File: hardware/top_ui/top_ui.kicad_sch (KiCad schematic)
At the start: 20 parts, among them J2 J_STK_A, J3 J_STK_B, J5 ST7789 240x280, J6 Stern Klinke, Q1 BC847, Q2 P-FET 20V 1A, SW1 BTN1, SW2 BTN2, SW3 BTN3, SW4 BTN4, U2 SHT40-AD1B, U3 VL53L1X

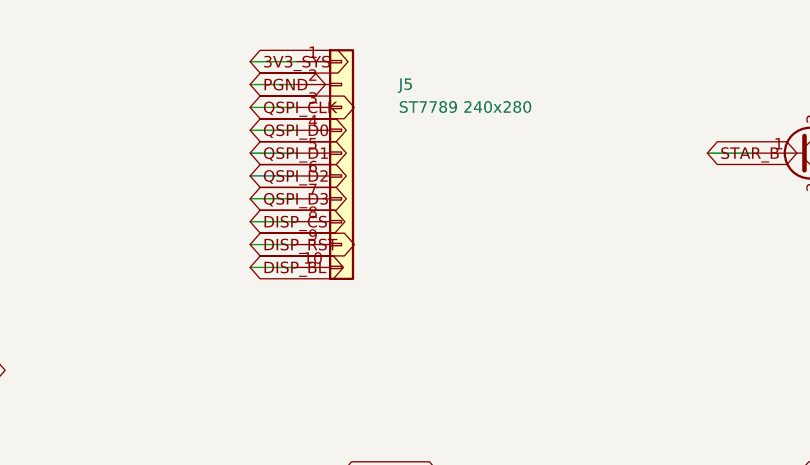
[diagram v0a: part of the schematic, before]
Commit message: Display gewaehlt: ER-TFT1.69-3, 12-polige FPC steckbar
  aktive Flaeche   27,97 x 32,63 mm
  sichtbar         28,97 x 33,63 mm
  Aussenmass       30,07 x 37,43 x 1,6 mm (FPC gefaltet)
  Treiber          ST7789V, 4-Draht-SPI

Quer eingebaut misst die aktive Flaeche 32,63 x 27,97 gegen ein Fenster von
32,70 x 27,00 - in der Breite bleiben 0,07 mm Luft, in der Hoehe verdeckt die
Zentralscheibe oben und unten je 0,49 mm. Rund acht Pixel je Seite, bewusst in
Kauf genommen. Die Firmware darf in diesen Zeilen nichts Wichtiges zeichnen.

Auf dem Top-Board passt es: 1,6 mm Dicke gegen 2,0 mm Budget, und in y reicht
das Panel nur bis +/-15,04 und bleibt damit frei von den Ecktastern bei
18,27..21,73. In x reicht es bis +/-18,71 und liegt NEBEN den Tastern, mit rund
1,5 mm diagonalem Abstand - das ist am realen Teil anzusehen.

J5 steht damit nicht mehr auf einem erfundenen 1,27-mm-Stiftleisten-Footprint
mit zehn Polen, sondern auf zwoelf Polen mit FPC-Buchse.

ZWEI ZAHLEN FEHLEN WEITERHIN, beide nur aus dem Datenblatt zu holen:

  Das RASTER der Fahne. Die Loetvariante ist mit 0,7 mm angegeben, und KiCad
  bringt fuer 0,7 mm kein einziges FPC-Footprint mit - nur 0,5 und 1,0. Ist es
  wirklich 0,7, muss eines in die Projektbibliothek gezeichnet werden. Bis
  dahin steht ein 0,5-mm-Footprint mit der richtigen Polzahl.

  Die PINBELEGUNG. Zwoelf Pole sind gesichert, welches Signal auf welchem
  liegt nicht. Die Zuordnung im Schaltplan ist die des alten Platzhalters und
  mit hoher Wahrscheinlichkeit falsch.

Beides steht so im Schaltplan-Generator, damit es niemand uebersieht: Solange
es offen ist, darf das Top-Board nicht bestellt werden.

Co-Authored-By: Claude Opus 5 (1M context) <noreply@anthropic.com>
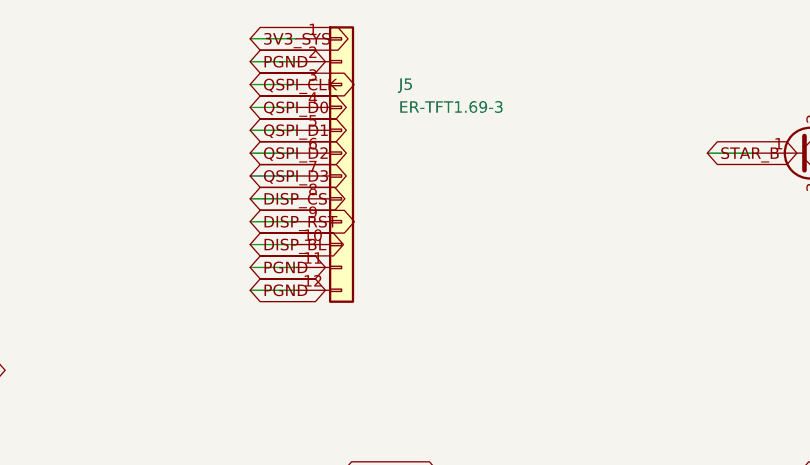
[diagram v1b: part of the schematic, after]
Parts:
- J5: value ST7789 240x280 -> ER-TFT1.69-3; footprint Connector_PinHeader_1.27mm:PinHeader_1x10_P1.27mm_Vertical -> Connector_FFC-FPC:TE_1-1734839-2_1x12-1MP_P0.5mm_Horizontal; symbol Connector_Generic:Conn_01x10 -> Connector_Generic:Conn_01x12; MPN PLATZHALTER - reales Modul mit FPC vermessen, dann Footprin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 -> Panel ER-TFT1.69-3, 12-pol FPC steckbar. RASTER UND PINBELE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
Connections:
- net PGND: now also J5.11 (Pin_11), J5.12 (Pin_12)

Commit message: Display nach Datenblatt verdrahtet - und die Beleuchtung bekommt einen Treiber
Das Datenblatt ER-TFT1.69-3 liegt vor, als Auszug gesichert in
docs/datasheets/. Zwei Dinge daraus aendern den Schaltplan.

DAS RASTER IST 0,50 mm, nicht 0,7 wie bei der Loetvariante. Das provisorisch
gewaehlte Footprint TE 1-1734839-2 stimmt also.

DIE PINBELEGUNG WAR KOMPLETT FALSCH. Sie stammte vom alten Platzhalter:

  war                        ist laut Datenblatt
  1 3V3   2 GND              1 TE     2 GND
  3 SCK   4 SDA              3 RS     4 RESET
  5 DC    6 frei             5 SDA    6 SCL
  7 frei  8 CS               7 CS     8 VCC
  9 RESET 10 BL              9 IOVCC  10 LEDA
  11 GND  12 GND             11 LEDK  12 GND

Kein einziger Pin lag richtig. Haette man so bestellt, waere 3,3 V auf den
TE-Ausgang des Displays gegangen und der Takt auf den Reset.

DIE HINTERGRUNDBELEUCHTUNG BRAUCHT EINEN TREIBER. Das Datenblatt nennt 45 mA
typisch und 60 mA maximal bei Vf = 3,0 bis 3,2 V, drei LEDs parallel. Bisher
hing LEDA direkt an DISP_BL - an einem GPIO des ESP32, ueber zwei
Steckkontakte des Stapels hinweg. Das haette den Pin ueberlastet.

Aus 3,3 V geht es auch mit Vorwiderstand nicht: Bei Vf zwischen 3,0 und 3,2 V
blieben 0,1 bis 0,3 V uebrig, der Strom schwankte um den Faktor drei allein
ueber die Bauteiltoleranz. Neu deshalb aus der 5-V-Schiene:

  R_BL   39 Ohm von 5V_SYS nach LEDA   (5,0-3,1)/45mA = 42 Ohm, 86 mW
  Q_BL   N-FET an der KATHODE, Gate an DISP_BL
  R_BLG  100k Pulldown - Beleuchtung aus, solange der ESP32 nicht bootet

Ohne den Pulldown leuchtet das Display beim Einschalten unkontrolliert auf.

  top_ui  20 -> 23 Bauteile, 52 -> 55 Netze

Co-Authored-By: Claude Opus 5 (1M context) <noreply@anthropic.com>
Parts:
- added Q_BL: N-FET 30V 1A, Package_TO_SOT_SMD:SOT-23, symbol SwitchStack:Q_NMOS_GDS
- added R_BL: 39R, Resistor_SMD:R_0603_1608Metric, symbol Device:R
- added R_BLG: 100k, Resistor_SMD:R_0603_1608Metric, symbol Device:R
- J5: MPN Panel ER-TFT1.69-3, 12-pol FPC steckbar. RASTER UND PINBELE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 -> Panel ER-TFT1.69-3, 12-pol FPC 0,50 mm steckbar - Raster un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
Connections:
- net 3V3_SYS: now also J5.8 (Pin_8), J5.9 (Pin_9); no longer J5.1 (Pin_1)
- net 5V_SYS: now also R_BL.1
- net DISP_BL: now also Q_BL.1 (G), R_BLG.1; no longer J5.10 (Pin_10)
- net DISP_CS: now also J5.7 (Pin_7); no longer J5.8 (Pin_8)
- net DISP_RST: now also J5.4 (Pin_4); no longer J5.9 (Pin_9)
- net PGND: now also Q_BL.3 (S), R_BLG.2; no longer J5.11 (Pin_11)
- net QSPI_CLK: now also J5.6 (Pin_6); no longer J5.3 (Pin_3)
- net QSPI_D0: now also J5.5 (Pin_5); no longer J5.4 (Pin_4)
- net QSPI_D1: now also J5.3 (Pin_3); no longer J5.5 (Pin_5)
- net QSPI_D2: no longer J5.6 (Pin_6)
- net QSPI_D3: no longer J5.7 (Pin_7)
- new net DISP_LEDA: J5.10 (Pin_10), R_BL.2
- new net DISP_LEDK: J5.11 (Pin_11), Q_BL.2 (D)
- new net DISP_TE: J5.1 (Pin_1)
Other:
- moved on the sheet: C2, C3, C4, F1, J2, J3, J6, Q1, Q2, R3, R4, R5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

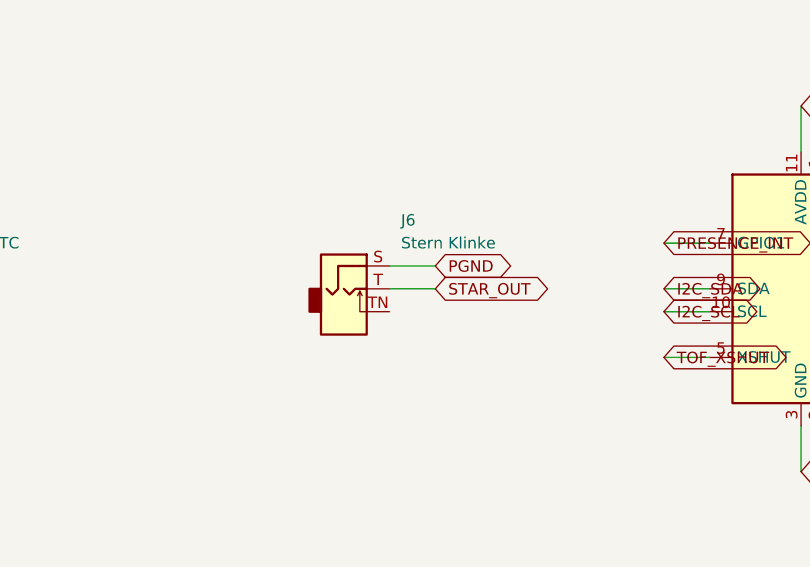
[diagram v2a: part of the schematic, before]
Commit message: Sternanschluss: JST GH statt Klinke, und die Panelflaeche wird gesperrt
DIE KLINKE PASSTE NICHT MEHR. Mit dem Displaypanel (30,07 x 37,43, mittig
ueber dem Scheibenfenster) bleibt darunter ein Streifen von 8,16 mm. Die
3,5-mm-Klinke misst 9,0 x 12,48 und braucht selbst quergelegt 9,0 mm.

Fuer zwei Litzen bei 80 mA war sie ohnehin ueberdimensioniert. Gemessen
wurden alle zweipoligen JST-Bauformen mit 3D-Modell:

  liegend  JST SH SM02B-SRSS-TB   2,96 mm hoch   passt unter die Scheibe
  stehend  JST GH BM02B-GHS-TBT   4,20 mm hoch   braucht eine Oeffnung
  stehend  JST SH BM02B-SRSS-TB   4,32 mm hoch
  stehend  JST PH B2B-PH-K        9,40 mm hoch

Ueber der Platine sind bis zur Scheibeninnenseite 3,50 mm frei - nur die
liegende SH bliebe ganz darunter.

GEWAEHLT: JST GH stehend, unten links bei (-10 / 19,4), mit einer Oeffnung
von rund 6 x 5 mm in der Zentralscheibe. Sie hat eine Verriegelung, und man
kommt ohne Abnehmen der Scheibe an den Stecker. Der Verbinder sitzt mit
0,73 mm Abstand zum Panel und 0,77 mm zum Boardrand.

DIE PANELFLAECHE IST JETZT GESPERRT. block_f deckt den Panelumriss plus
0,5 mm Klebefuge ab - vorher wanderte der Stern-P-FET mit einer Ecke
hinein, und vor dem Seitenwechsel standen dort die Stackverbinder.

BEFESTIGUNG DES PANELS in docs/04 festgehalten: geklebt auf die
Platinenvorderseite, umlaufend auf den Rand ausserhalb der aktiven Flaeche
(2,40 mm lange Seite, 1,05 mm kurze). Die Schaumdichtung fuellt die 1,90 mm
zur Scheibe, drueckt an und haelt Staub ab - darf aber NICHT die Befestigung
sein, denn die Scheibe ist wegen USB bewusst abnehmbar.

Co-Authored-By: Claude Opus 5 (1M context) <noreply@anthropic.com>
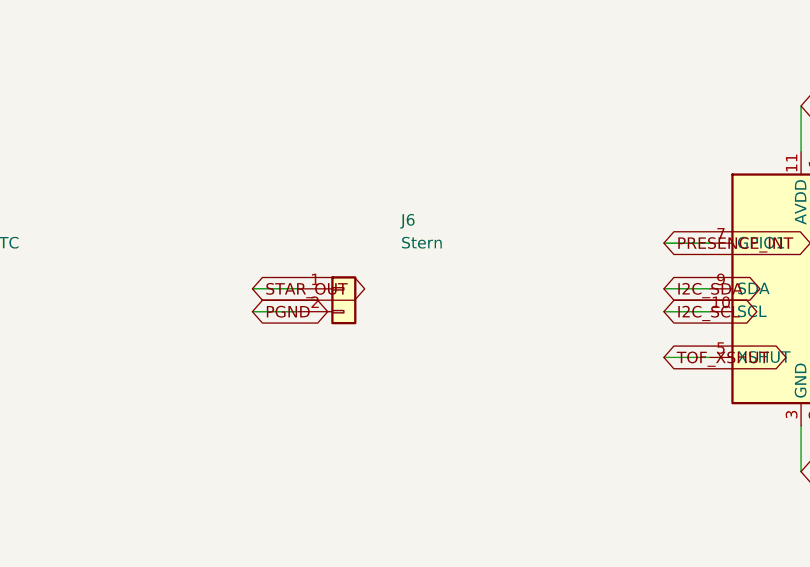
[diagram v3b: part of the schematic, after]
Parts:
- J6: value Stern Klinke -> Stern; footprint Connector_Audio:Jack_3.5mm_QingPu_WQP-PJ398SM_Vertical_CircularHoles -> Connector_JST:JST_GH_BM02B-GHS-TBT_1x02-1MP_P1.25mm_Vertical; symbol Connector_Audio:AudioJack2_SwitchT -> Connector_Generic:Conn_01x02; MPN PLATZHALTER 3,5 mm vertikal - Zielteil 2,5 mm, Bauhoehe max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 -> JST GH BM02B-GHS-TBT, 2-polig stehend mit Verriegelung
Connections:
- net PGND: now also J6.2 (Pin_2); no longer J6.S
- net STAR_OUT: now also J6.1 (Pin_1); no longer J6.T
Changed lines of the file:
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@@
       (reference "F1") (unit 1))))
   )
-  (symbol (lib_id "Connector_Audio:AudioJack2_SwitchT") (at 381.0000 69.8500 0) (unit 1)
+  (symbol (lib_id "Connector_Generic:Conn_01x02") (at 381.0000 69.8500 0) (unit 1)
     (in_bom yes) (on_board yes) (dnp no)
     (property "Reference" "J6" (at 387.3500 62.2300 0)
       (effects (font (size 1.27 1.27)) (justify left)))
-    (property "Value" "Stern Klinke" (at 387.3500 64.7700 0)
-      (effects (font (size 1.27 1.27)) (justify left)))
-    (property "Footprint" "Connector_Audio:Jack_3.5mm_QingPu_WQP-PJ398SM_Vertical_CircularHoles" (at 381.0000 69.8500 0)
-      (effects (font (size 1.27 1.27)) hide))
-    (property "MPN" "PLATZHALTER 3,5 mm vertikal - Zielteil 2,5 mm, Bauhoehe max 10,5 mm ueber der Platine, Footprint aus dem Datenblatt uebernehmen" (at 381.0000 72.3900 0)
-      (effects (font (size 1.27 1.27)) hide))
-    (pin "S")
-    (pin "T")
-    (pin "TN")
+    (property "Value" "Stern" (at 387.3500 64.7700 0)
+      (effects (font (size 1.27 1.27)) (justify left)))
+    (property "Footprint" "Connector_JST:JST_GH_BM02B-GHS-TBT_1x02-1MP_P1.25mm_Vertical" (at 381.0000 69.8500 0)
+      (effects (font (size 1.27 1.27)) hide))
+    (property "MPN" "JST GH BM02B-GHS-TBT, 2-polig stehend mit Verriegelung" (at 381.0000 72.3900 0)
+      (effects (font (size 1.27 1.27)) hide))
+    (pin "1")
+    (pin "2")
     (instances (project "top_ui" (path "/b42c7d3a-b5ea-559e-28b6-972545138727"
       (reference "J6") (unit 1))))
@@
     (effects (font (size 1.27 1.27)) (justify left))
     (property "Intersheetrefs" "${INTERSHEET_REFS}" (at 279.4000 78.7400 0) (effects (font (size 1.27 1.27)) hide)))
-  (wire (pts (xy 386.0800 67.3100) (xy 391.1600 67.3100))
-    (stroke (width 0) (type default)))
-  (global_label "PGND" (shape bidirectional) (at 391.1600 67.3100 0)
-    (effects (font (size 1.27 1.27)) (justify left))
-    (property "Intersheetrefs" "${INTERSHEET_REFS}" (at 391.1600 67.3100 0) (effects (font (size 1.27 1.27)) hide)))
+  (wire (pts (xy 375.9200 72.3900) (xy 370.8400 72.3900))
+    (stroke (width 0) (type default)))
+  (global_label "PGND" (shape bidirectional) (at 370.8400 72.3900 0)
+    (effects (font (size 1.27 1.27)) (justify left))
+    (property "Intersheetrefs" "${INTERSHEET_REFS}" (at 370.8400 72.3900 0) (effects (font (size 1.27 1.27)) hide)))
   (wire (pts (xy 434.3400 85.0900) (xy 434.3400 90.1700))
     (stroke (width 0) (type default)))
@@
     (effects (font (size 1.27 1.27)) (justify left))
     (property "Intersheetrefs" "${INTERSHEET_REFS}" (at 330.2000 78.7400 0) (effects (font (size 1.27 1.27)) hide)))
-  (wire (pts (xy 386.0800 69.8500) (xy 391.1600 69.8500))
-    (stroke (width 0) (type default)))
-  (global_label "STAR_OUT" (shape bidirectional) (at 391.1600 69.8500 0)
-    (effects (font (size 1.27 1.27)) (justify left))
-    (property "Intersheetrefs" "${INTERSHEET_REFS}" (at 391.1600 69.8500 0) (effects (font (size 1.27 1.27)) hide)))
+  (wire (pts (xy 375.9200 69.8500) (xy 370.8400 69.8500))
+    (stroke (width 0) (type default)))
+  (global_label "STAR_OUT" (shape bidirectional) (at 370.8400 69.8500 0)
+    (effects (font (size 1.27 1.27)) (justify left))
+    (property "Intersheetrefs" "${INTERSHEET_REFS}" (at 370.8400 69.8500 0) (effects (font (size 1.27 1.27)) hide)))
   (wire (pts (xy 279.4000 66.0400) (xy 279.4000 60.9600))
     (stroke (width 0) (type default)))
